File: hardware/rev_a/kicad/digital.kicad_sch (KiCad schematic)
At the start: 15 parts, among them J1 TSW-110-07-T-D, U1 ADS1299-4PAGR

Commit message: fix(hardware): migrate both bench headers to the high-temperature HTSW selection
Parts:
- J1: value TSW-110-07-T-D -> HTSW-110-07-T-D; MPN TSW-110-07-T-D -> HTSW-110-07-T-D
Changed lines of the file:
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@@
 (in_bom yes) (on_board yes) (dnp no)
 (property "Reference" "J1" (at 355.6 57.15 0) (effects (font (size 1.27 1.27))))
-(property "Value" "TSW-110-07-T-D" (at 355.6 59.69 0) (effects (font (size 1.27 1.27))))
+(property "Value" "HTSW-110-07-T-D" (at 355.6 59.69 0) (effects (font (size 1.27 1.27))))
 (property "Footprint" "Connector_PinHeader_2.54mm:PinHeader_2x10_P2.54mm_Vertical" (at 355.6 88.9 0) (effects (font (size 1.27 1.27)) (hide yes)))
 (property "Datasheet" "" (at 355.6 88.9 0) (effects (font (size 1.27 1.27)) (hide yes)))
 (property "ContractRef" "J_DIG" (at 355.6 88.9 0) (effects (font (size 1.27 1.27)) (hide yes)))
-(property "MPN" "TSW-110-07-T-D" (at 355.6 88.9 0) (effects (font (size 1.27 1.27)) (hide yes)))
+(property "MPN" "HTSW-110-07-T-D" (at 355.6 88.9 0) (effects (font (size 1.27 1.27)) (hide yes)))
 (property "BOM_ID" "headers" (at 355.6 88.9 0) (effects (font (size 1.27 1.27)) (hide yes)))
 (property "Population" "fit" (at 355.6 88.9 0) (effects (font (size 1.27 1.27)) (hide yes)))

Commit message: feat(hardware): author C3 native auxiliary and migrate loaded bus pulls
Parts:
- R12, R13, R15, R16, R17, R18, R19: value 10k -> 42.2k; BOM_ID straps -> bus_pulldowns; MPN RC0603FR-0710KL -> RC0603FR-0742K2L
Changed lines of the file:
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@@
 (in_bom yes) (on_board yes) (dnp no)
 (property "Reference" "R12" (at 49.53 185.42 90) (effects (font (size 1.27 1.27))))
-(property "Value" "10k" (at 49.53 189.23 90) (effects (font (size 1.27 1.27))))
+(property "Value" "42.2k" (at 49.53 189.23 90) (effects (font (size 1.27 1.27))))
 (property "Footprint" "Resistor_SMD:R_0603_1608Metric" (at 40.64 187.96 0) (effects (font (size 1.27 1.27)) (hide yes)))
 (property "Datasheet" "" (at 40.64 187.96 0) (effects (font (size 1.27 1.27)) (hide yes)))
 (property "ContractRef" "R_CS_DN" (at 40.64 187.96 0) (effects (font (size 1.27 1.27)) (hide yes)))
-(property "MPN" "RC0603FR-0710KL" (at 40.64 187.96 0) (effects (font (size 1.27 1.27)) (hide yes)))
-(property "BOM_ID" "straps" (at 40.64 187.96 0) (effects (font (size 1.27 1.27)) (hide yes)))
+(property "MPN" "RC0603FR-0742K2L" (at 40.64 187.96 0) (effects (font (size 1.27 1.27)) (hide yes)))
+(property "BOM_ID" "bus_pulldowns" (at 40.64 187.96 0) (effects (font (size 1.27 1.27)) (hide yes)))
 (property "Population" "fit" (at 40.64 187.96 0) (effects (font (size 1.27 1.27)) (hide yes)))
 (property "Tolerance" "0.01" (at 40.64 187.96 0) (effects (font (size 1.27 1.27)) (hide yes)))
@@
 (in_bom yes) (on_board yes) (dnp no)
 (property "Reference" "R13" (at 107.95 185.42 90) (effects (font (size 1.27 1.27))))
-(property "Value" "10k" (at 107.95 189.23 90) (effects (font (size 1.27 1.27))))
+(property "Value" "42.2k" (at 107.95 189.23 90) (effects (font (size 1.27 1.27))))
 (property "Footprint" "Resistor_SMD:R_0603_1608Metric" (at 99.06 187.96 0) (effects (font (size 1.27 1.27)) (hide yes)))
 (property "Datasheet" "" (at 99.06 187.96 0) (effects (font (size 1.27 1.27)) (hide yes)))
 (property "ContractRef" "R_CLKSEL_DN" (at 99.06 187.96 0) (effects (font (size 1.27 1.27)) (hide yes)))
-(property "MPN" "RC0603FR-0710KL" (at 99.06 187.96 0) (effects (font (size 1.27 1.27)) (hide yes)))
-(property "BOM_ID" "straps" (at 99.06 187.96 0) (effects (font (size 1.27 1.27)) (hide yes)))
+(property "MPN" "RC0603FR-0742K2L" (at 99.06 187.96 0) (effects (font (size 1.27 1.27)) (hide yes)))
+(property "BOM_ID" "bus_pulldowns" (at 99.06 187.96 0) (effects (font (size 1.27 1.27)) (hide yes)))
 (property "Population" "fit" (at 99.06 187.96 0) (effects (font (size 1.27 1.27)) (hide yes)))
 (property "Tolerance" "0.01" (at 99.06 187.96 0) (effects (font (size 1.27 1.27)) (hide yes)))
@@
 (in_bom yes) (on_board yes) (dnp no)
 (property "Reference" "R15" (at 224.79 185.42 90) (effects (font (size 1.27 1.27))))
-(property "Value" "10k" (at 224.79 189.23 90) (effects (font (size 1.27 1.27))))
+(property "Value" "42.2k" (at 224.79 189.23 90) (effects (font (size 1.27 1.27))))
 (property "Footprint" "Resistor_SMD:R_0603_1608Metric" (at 215.9 187.96 0) (effects (font (size 1.27 1.27)) (hide yes)))
 (property "Datasheet" "" (at 215.9 187.96 0) (effects (font (size 1.27 1.27)) (hide yes)))
 (property "ContractRef" "R_RESET_DN" (at 215.9 187.96 0) (effects (font (size 1.27 1.27)) (hide yes)))
-(property "MPN" "RC0603FR-0710KL" (at 215.9 187.96 0) (effects (font (size 1.27 1.27)) (hide yes)))
-(property "BOM_ID" "straps" (at 215.9 187.96 0) (effects (font (size 1.27 1.27)) (hide yes)))
+(property "MPN" "RC0603FR-0742K2L" (at 215.9 187.96 0) (effects (font (size 1.27 1.27)) (hide yes)))
+(property "BOM_ID" "bus_pulldowns" (at 215.9 187.96 0) (effects (font (size 1.27 1.27)) (hide yes)))
 (property "Population" "fit" (at 215.9 187.96 0) (effects (font (size 1.27 1.27)) (hide yes)))
 (property "Tolerance" "0.01" (at 215.9 187.96 0) (effects (font (size 1.27 1.27)) (hide yes)))
@@
 (in_bom yes) (on_board yes) (dnp no)
 (property "Reference" "R16" (at 283.21 185.42 90) (effects (font (size 1.27 1.27))))
-(property "Value" "10k" (at 283.21 189.23 90) (effects (font (size 1.27 1.27))))
+(property "Value" "42.2k" (at 283.21 189.23 90) (effects (font (size 1.27 1.27))))
 (property "Footprint" "Resistor_SMD:R_0603_1608Metric" (at 274.32 187.96 0) (effects (font (size 1.27 1.27)) (hide yes)))
 (property "Datasheet" "" (at 274.32 187.96 0) (effects (font (size 1.27 1.27)) (hide yes)))
 (property "ContractRef" "R_PWDN_DN" (at 274.32 187.96 0) (effects (font (size 1.27 1.27)) (hide yes)))
-(property "MPN" "RC0603FR-0710KL" (at 274.32 187.96 0) (effects (font (size 1.27 1.27)) (hide yes)))
-(property "BOM_ID" "straps" (at 274.32 187.96 0) (effects (font (size 1.27 1.27)) (hide yes)))
+(property "MPN" "RC0603FR-0742K2L" (at 274.32 187.96 0) (effects (font (size 1.27 1.27)) (hide yes)))
+(property "BOM_ID" "bus_pulldowns" (at 274.32 187.96 0) (effects (font (size 1.27 1.27)) (hide yes)))
 (property "Population" "fit" (at 274.32 187.96 0) (effects (font (size 1.27 1.27)) (hide yes)))
 (property "Tolerance" "0.01" (at 274.32 187.96 0) (effects (font (size 1.27 1.27)) (hide yes)))
@@
 (in_bom yes) (on_board yes) (dnp no)
 (property "Reference" "R17" (at 341.63 185.42 90) (effects (font (size 1.27 1.27))))
-(property "Value" "10k" (at 341.63 189.23 90) (effects (font (size 1.27 1.27))))
+(property "Value" "42.2k" (at 341.63 189.23 90) (effects (font (size 1.27 1.27))))
 (property "Footprint" "Resistor_SMD:R_0603_1608Metric" (at 332.74 187.96 0) (effects (font (size 1.27 1.27)) (hide yes)))
 (property "Datasheet" "" (at 332.74 187.96 0) (effects (font (size 1.27 1.27)) (hide yes)))
 (property "ContractRef" "R_START_DN" (at 332.74 187.96 0) (effects (font (size 1.27 1.27)) (hide yes)))
-(property "MPN" "RC0603FR-0710KL" (at 332.74 187.96 0) (effects (font (size 1.27 1.27)) (hide yes)))
-(property "BOM_ID" "straps" (at 332.74 187.96 0) (effects (font (size 1.27 1.27)) (hide yes)))
+(property "MPN" "RC0603FR-0742K2L" (at 332.74 187.96 0) (effects (font (size 1.27 1.27)) (hide yes)))
+(property "BOM_ID" "bus_pulldowns" (at 332.74 187.96 0) (effects (font (size 1.27 1.27)) (hide yes)))
 (property "Population" "fit" (at 332.74 187.96 0) (effects (font (size 1.27 1.27)) (hide yes)))
 (property "Tolerance" "0.01" (at 332.74 187.96 0) (effects (font (size 1.27 1.27)) (hide yes)))
@@
 (in_bom yes) (on_board yes) (dnp no)
 (property "Reference" "R18" (at 49.53 226.06 90) (effects (font (size 1.27 1.27))))
-(property "Value" "10k" (at 49.53 229.87 90) (effects (font (size 1.27 1.27))))
+(property "Value" "42.2k" (at 49.53 229.87 90) (effects (font (size 1.27 1.27))))
 (property "Footprint" "Resistor_SMD:R_0603_1608Metric" (at 40.64 228.6 0) (effects (font (size 1.27 1.27)) (hide yes)))
 (property "Datasheet" "" (at 40.64 228.6 0) (effects (font (size 1.27 1.27)) (hide yes)))
 (property "ContractRef" "R_SCLK_DN" (at 40.64 228.6 0) (effects (font (size 1.27 1.27)) (hide yes)))
-(property "MPN" "RC0603FR-0710KL" (at 40.64 228.6 0) (effects (font (size 1.27 1.27)) (hide yes)))
-(property "BOM_ID" "straps" (at 40.64 228.6 0) (effects (font (size 1.27 1.27)) (hide yes)))
+(property "MPN" "RC0603FR-0742K2L" (at 40.64 228.6 0) (effects (font (size 1.27 1.27)) (hide yes)))
+(property "BOM_ID" "bus_pulldowns" (at 40.64 228.6 0) (effects (font (size 1.27 1.27)) (hide yes)))
 (property "Population" "fit" (at 40.64 228.6 0) (effects (font (size 1.27 1.27)) (hide yes)))
 (property "Tolerance" "0.01" (at 40.64 228.6 0) (effects (font (size 1.27 1.27)) (hide yes)))
@@
 (in_bom yes) (on_board yes) (dnp no)
 (property "Reference" "R19" (at 107.95 226.06 90) (effects (font (size 1.27 1.27))))
-(property "Value" "10k" (at 107.95 229.87 90) (effects (font (size 1.27 1.27))))
+(property "Value" "42.2k" (at 107.95 229.87 90) (effects (font (size 1.27 1.27))))
 (property "Footprint" "Resistor_SMD:R_0603_1608Metric" (at 99.06 228.6 0) (effects (font (size 1.27 1.27)) (hide yes)))
 (property "Datasheet" "" (at 99.06 228.6 0) (effects (font (size 1.27 1.27)) (hide yes)))
 (property "ContractRef" "R_DIN_DN" (at 99.06 228.6 0) (effects (font (size 1.27 1.27)) (hide yes)))
-(property "MPN" "RC0603FR-0710KL" (at 99.06 228.6 0) (effects (font (size 1.27 1.27)) (hide yes)))
-(property "BOM_ID" "straps" (at 99.06 228.6 0) (effects (font (size 1.27 1.27)) (hide yes)))
+(property "MPN" "RC0603FR-0742K2L" (at 99.06 228.6 0) (effects (font (size 1.27 1.27)) (hide yes)))
+(property "BOM_ID" "bus_pulldowns" (at 99.06 228.6 0) (effects (font (size 1.27 1.27)) (hide yes)))
 (property "Population" "fit" (at 99.06 228.6 0) (effects (font (size 1.27 1.27)) (hide yes)))
 (property "Tolerance" "0.01" (at 99.06 228.6 0) (effects (font (size 1.27 1.27)) (hide yes)))

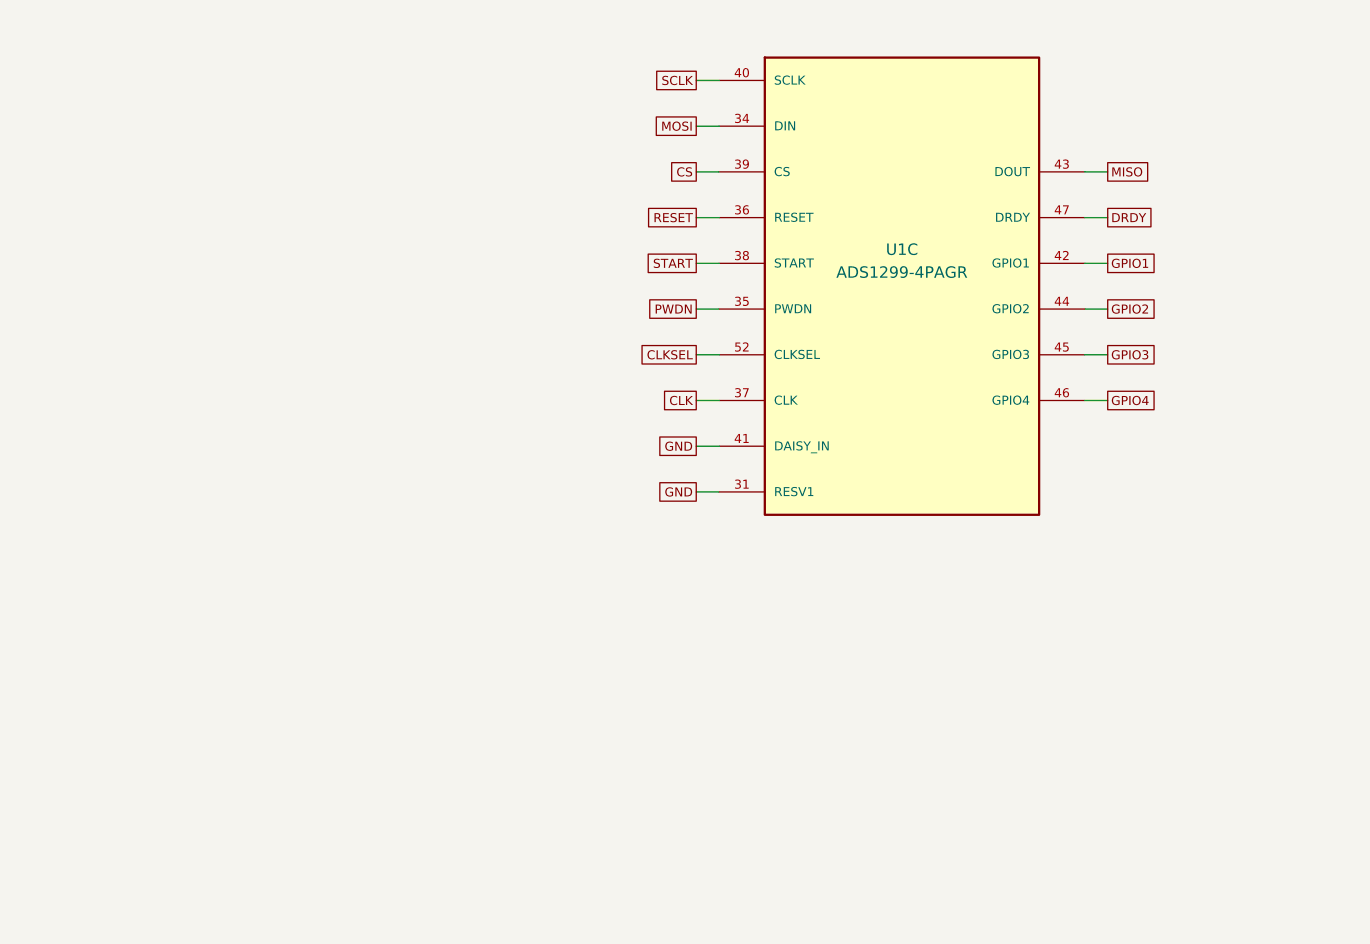
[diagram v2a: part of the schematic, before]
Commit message: feat(hardware): apply the preserved five-position SPI source candidate
Apply exactly eleven manifest-verified files on 08a8ddd0, retaining
all later DNP, preservation, selection and native-fault test repairs.
The historical patch reproduces 2e50d2b; no geometry is recreated.
Five positions remain DNP/NOT_SELECTED. Native exports and copper
fills are not refreshed here. This is source publication only, not
a passing gate, approved damping value or fabrication release.
No workflow, firmware, Q1, dependency or permission setting changes
are included in this engineering commit. No project code executed
by the isolated source publisher. PR98 must remain draft.
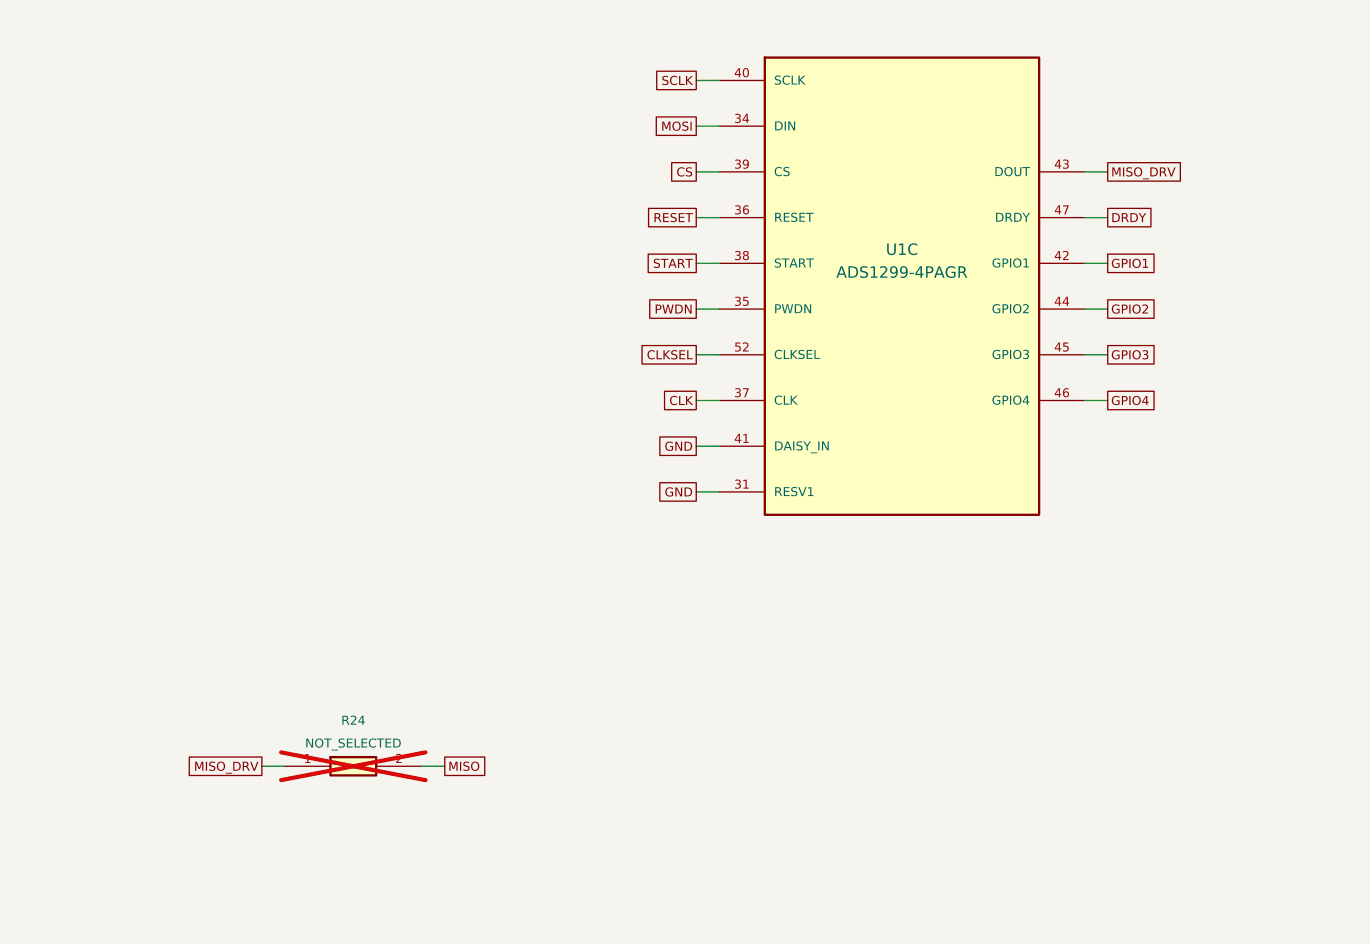
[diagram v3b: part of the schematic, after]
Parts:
- added R24: NOT_SELECTED, Resistor_SMD:R_0603_1608Metric, symbol RevA:R
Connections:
- net MISO: now also R24.2; no longer U1.43 (DOUT)
- new net MISO_DRV: R24.1, U1.43 (DOUT)
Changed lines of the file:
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@@
 (global_label "GND" (shape passive) (at 228.6 111.76 180) (effects (font (size 1.0 1.0)) (justify right)))
 (wire (pts (xy 271.78 76.2) (xy 274.32 76.2)) (stroke (width 0) (type default)))
-(global_label "MISO" (shape passive) (at 274.32 76.2 0) (effects (font (size 1.0 1.0)) (justify left)))
+(global_label "MISO_DRV" (shape passive) (at 274.32 76.2 0) (effects (font (size 1.0 1.0)) (justify left)))
 (wire (pts (xy 271.78 81.28) (xy 274.32 81.28)) (stroke (width 0) (type default)))
 (global_label "DRDY" (shape passive) (at 274.32 81.28 0) (effects (font (size 1.0 1.0)) (justify left)))
@@
 (text "CS, RESET and PWDN are active-low controls. This is a bench review candidate, not a released interface." (at 15.24 262.89 0) (effects (font (size 1.27 1.27)) (justify left)))
 (sheet_instances (path "/" (page "3")))
-)
+(symbol (lib_id "RevA:R") (at 190.5 142.24 0) (unit 1) (in_bom yes) (on_board yes) (dnp yes)
+(property "Reference" "R24" (at 190.5 137.16 0) (effects (font (size 1 1))))
+(property "Value" "NOT_SELECTED" (at 190.5 139.7 0) (effects (font (size 1 1))))
+(property "Footprint" "Resistor_SMD:R_0603_1608Metric" (at 190.5 142.24 0) (effects (font (size 1 1)) (hide yes)))
+(property "Datasheet" "" (at 190.5 142.24 0) (effects (font (size 1 1)) (hide yes)))
+(property "ContractRef" "R_MISO_SER" (at 190.5 142.24 0) (effects (font (size 1 1)) (hide yes)))
+(property "MPN" "NOT_SELECTED" (at 190.5 142.24 0) (effects (font (size 1 1)) (hide yes)))
+(property "Population" "dnp" (at 190.5 142.24 0) (effects (font (size 1 1)) (hide yes)))
+(property "BOM_ID" "spi_series" (at 190.5 142.24 0) (effects (font (size 1 1)) (hide yes)))
+(pin "1")
+(pin "2")
+(instances (project "rev_a" (path "/6426aeea-facb-56f2-ae10-495fdfe5ecae/acfb31a8-7d12-5bff-9d10-ce4fab1bc9c7" (reference "R24") (unit 1)))) )
+(wire (pts (xy 182.88 142.24) (xy 180.34 142.24)) (stroke (width 0) (type default)))
+(global_label "MISO_DRV" (shape passive) (at 180.34 142.24 180) (effects (font (size 1 1)) (justify right)))
+(wire (pts (xy 198.12 142.24) (xy 200.66 142.24)) (stroke (width 0) (type default)))
+(global_label "MISO" (shape passive) (at 200.66 142.24 0) (effects (font (size 1 1)) (justify left)))
+)
